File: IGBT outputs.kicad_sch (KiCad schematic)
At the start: 8 parts, among them Q1 NGD8201AN, Q2 NGD8201AN, Q3 NGD8201AN, Q4 NGD8201AN, Q5 NGD8201AN, Q6 NGD8201AN, Q7 NGD8201AN, Q8 NGD8201AN

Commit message: BOM cleanup, minor USB improvements, bump to 1.2
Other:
- company: FutureProofPerformance.com -> github.com/FOME-Tech
- title: Polygonus Universal 88p -> FOME Universal 112 pin ECU base
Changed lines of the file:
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@@
 	(paper "A4")
 	(title_block
-		(title "Polygonus Universal 88p")
-		(date "2023-11-12")
-		(rev "v1.0")
-		(company "FutureProofPerformance.com")
+		(title "FOME Universal 112 pin ECU base")
+		(date "2026-03-03")
+		(rev "v1.2")
+		(company "github.com/FOME-Tech")
+		(comment 1 "FutureProofPerformance.com")
+		(comment 2 "happycactusgarage.com")
 	)
 	(wire

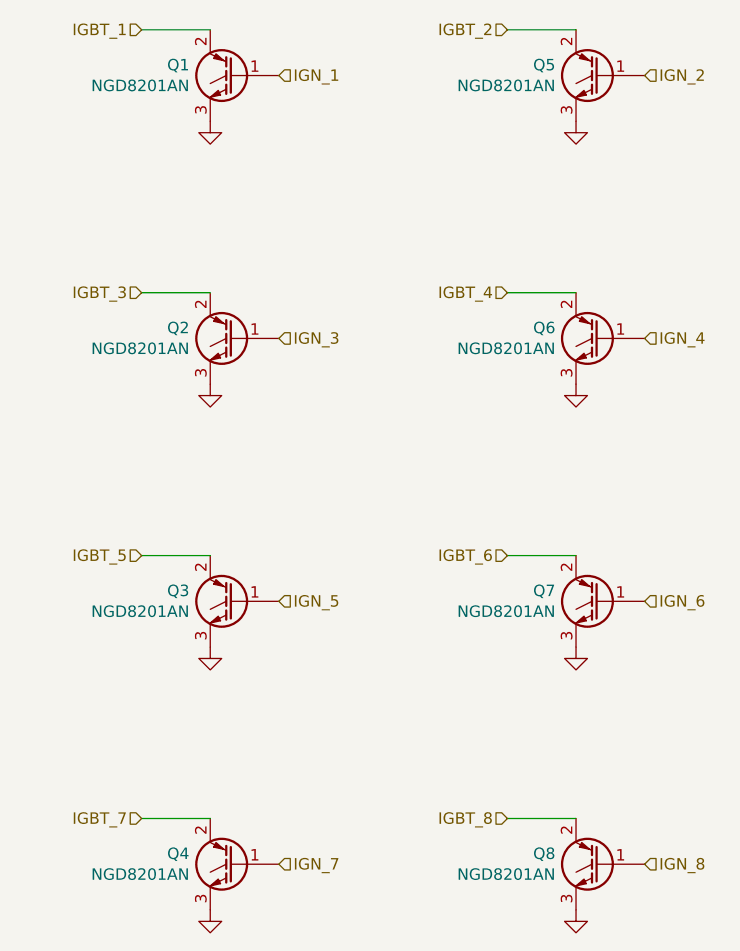
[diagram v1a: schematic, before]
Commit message: more BOM optimization
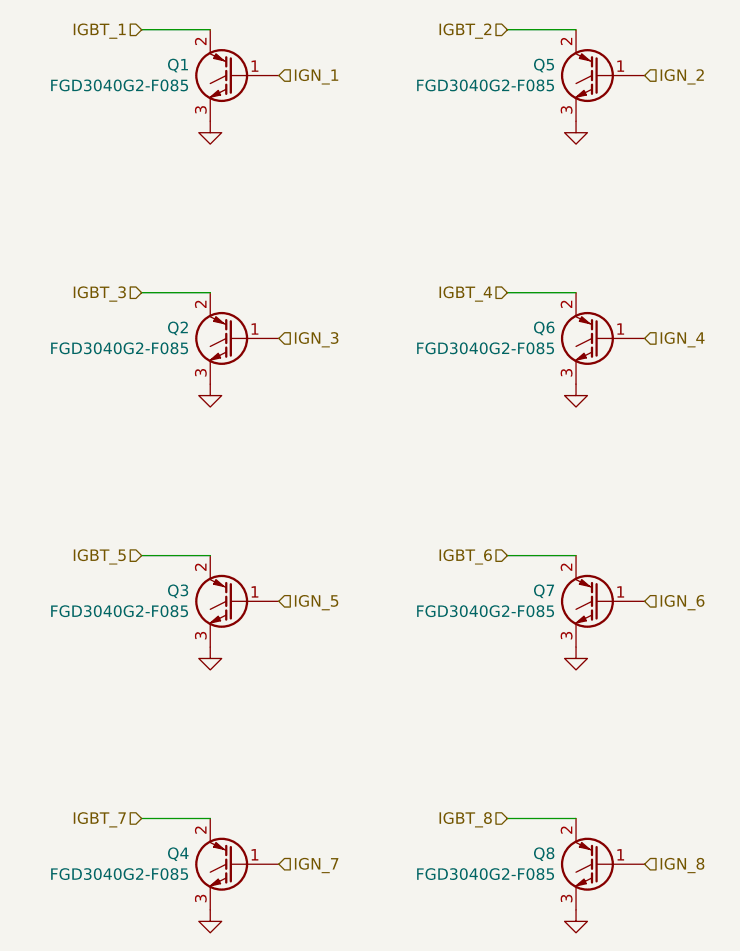
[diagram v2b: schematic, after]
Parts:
- Q1, Q2, Q3, Q4, Q5, Q6, Q7, Q8: value NGD8201AN -> FGD3040G2-F085; LCSC C151649 -> C606124
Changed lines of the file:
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@@
 			)
 		)
-		(property "Value" "NGD8201AN"
+		(property "Value" "FGD3040G2-F085"
 			(at 176.7586 135.763 0)
 			(effects
@@
 			)
 		)
-		(property "LCSC" "C151649"
+		(property "LCSC" "C606124"
 			(at 181.61 134.62 0)
 			(effects
@@
 			)
 		)
-		(property "Value" "NGD8201AN"
+		(property "Value" "FGD3040G2-F085"
 			(at 217.424 77.343 0)
 			(effects
@@
 			)
 		)
-		(property "LCSC" "C151649"
+		(property "LCSC" "C606124"
 			(at 222.25 76.2 0)
 			(effects
@@
 			)
 		)
-		(property "Value" "NGD8201AN"
+		(property "Value" "FGD3040G2-F085"
 			(at 176.7586 48.133 0)
 			(effects
@@
 			)
 		)
-		(property "LCSC" "C151649"
+		(property "LCSC" "C606124"
 			(at 181.61 46.99 0)
 			(effects
@@
 			)
 		)
-		(property "Value" "NGD8201AN"
+		(property "Value" "FGD3040G2-F085"
 			(at 176.7586 106.553 0)
 			(effects
@@
 			)
 		)
-		(property "LCSC" "C151649"
+		(property "LCSC" "C606124"
 			(at 181.61 105.41 0)
 			(effects
@@
 			)
 		)
-		(property "Value" "NGD8201AN"
+		(property "Value" "FGD3040G2-F085"
 			(at 176.7586 77.343 0)
 			(effects
@@
 			)
 		)
-		(property "LCSC" "C151649"
+		(property "LCSC" "C606124"
 			(at 181.61 76.2 0)
 			(effects
@@
 			)
 		)
-		(property "Value" "NGD8201AN"
+		(property "Value" "FGD3040G2-F085"
 			(at 217.424 106.553 0)
 			(effects
@@
 			)
 		)
-		(property "LCSC" "C151649"
+		(property "LCSC" "C606124"
 			(at 222.25 105.41 0)
 			(effects
@@
 			)
 		)
-		(property "Value" "NGD8201AN"
+		(property "Value" "FGD3040G2-F085"
 			(at 217.424 48.133 0)
 			(effects
@@
 			)
 		)
-		(property "LCSC" "C151649"
+		(property "LCSC" "C606124"
 			(at 222.25 46.99 0)
 			(effects
@@
 			)
 		)
-		(property "Value" "NGD8201AN"
+		(property "Value" "FGD3040G2-F085"
 			(at 217.424 135.763 0)
 			(effects
@@
 			)
 		)
-		(property "LCSC" "C151649"
+		(property "LCSC" "C606124"
 			(at 222.25 134.62 0)
 			(effects
